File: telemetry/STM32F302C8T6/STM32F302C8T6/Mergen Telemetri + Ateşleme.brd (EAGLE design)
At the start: 49.7 x 87.5 mm, 91 parts, among them J2 U.FL, Q2 IRLML6344TRPBF, Q3 IRLML6344TRPBF, U2 BMP280, U3 MPU-6050, U4 L86, U6 AMS1117-3.3, U7 AMS1117-3.3, U8 STM32F302C8T6, X1 JST-XH-04-PIN-LONG-PAD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

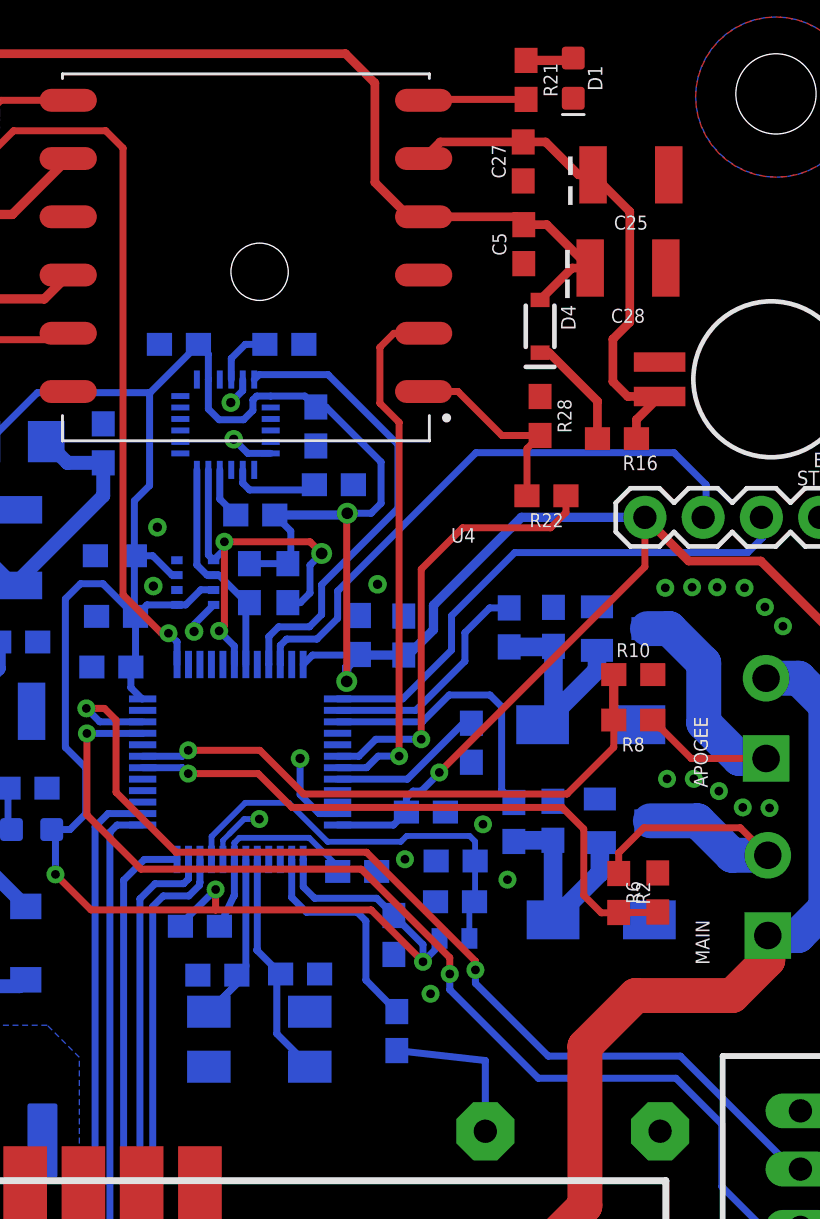
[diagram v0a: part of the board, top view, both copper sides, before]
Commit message: packages was modified according to stock situation
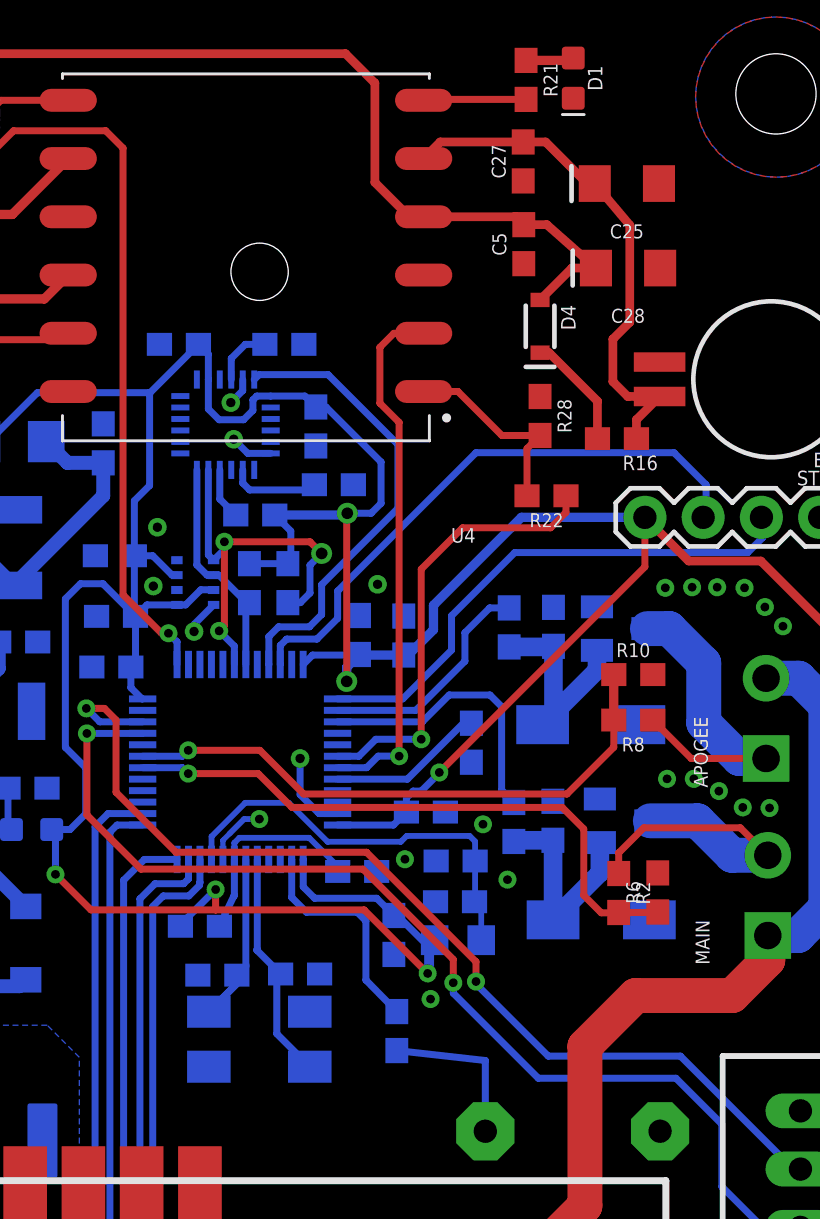
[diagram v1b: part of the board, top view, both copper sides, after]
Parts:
- C25, C28: device SparkFun-Capacitors:EIA3528 -> SparkFun-Capacitors:EIA3216
- L2: value BLM15HB221SN1 -> (none); device inductors:0402 -> 52101-101-REV-A_v16:RC-MASTER-SMD_L0805MP
- R30, R4: value 20 -> 22
- moved C25 0.42 mm to (73.5, 57.2)
- moved L2 0.17 mm to (66.2, 24.2)
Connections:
- net 3.3V: now also C28.+; no longer C28.A
- net GND: now also C25.-, C28.-; no longer C25.C, C28.C
- net V_BCKP: now also C25.+; no longer C25.A
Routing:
- net 3.3V: track 252.0 -> 253.9 mm
